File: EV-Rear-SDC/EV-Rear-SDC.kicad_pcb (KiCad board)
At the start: 2 copper layers, 0 parts

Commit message: Moved Mosfet to avoid EMI error
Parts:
- added C1: 0.1u, Capacitor_SMD:C_0805_2012Metric, F.Cu at (104.6, 125.0)
- added C2: 0.1u, Capacitor_SMD:C_0805_2012Metric, F.Cu at (85.0, 131.6)
- added C3: 1u, Capacitor_SMD:C_0805_2012Metric, F.Cu at (104.7, 128.7)
- added C4: 10u, Capacitor_SMD:C_0805_2012Metric, F.Cu at (85.1, 134.9)
- added C5: 1u, Capacitor_SMD:C_0805_2012Metric, F.Cu at (104.7, 132.3)
- added C6: 0.1u, Capacitor_SMD:C_0805_2012Metric, F.Cu at (73.8, 121.4)
- added C7: 0.1u, Capacitor_SMD:C_0805_2012Metric, F.Cu at (101.2, 116.8)
- added C8: 1u, Capacitor_SMD:C_0805_2012Metric, F.Cu at (101.3, 120.2)
- added C9: 0.1u, Capacitor_SMD:C_0805_2012Metric, F.Cu at (85.0, 117.7)
- added D1: LED, LED_SMD:LED_0805_2012Metric, F.Cu at (87.3, 109.5)
- added D2: LED, LED_SMD:LED_0805_2012Metric, F.Cu at (77.0, 109.1)
- added D3: LED, LED_SMD:LED_0805_2012Metric, F.Cu at (70.3, 109.2)
- added D4: LED, LED_SMD:LED_0805_2012Metric, F.Cu at (66.6, 121.4)
- added D5: LED, LED_SMD:LED_0805_2012Metric, F.Cu at (66.6, 128.7)
- added D6: D, Diode_SMD:D_0805_2012Metric, F.Cu at (105.0, 143.2)
- added D7: LED, LED_SMD:LED_0805_2012Metric, F.Cu at (66.2, 135.5)
- added D8: LED, LED_SMD:LED_0805_2012Metric, F.Cu at (76.1, 133.7)
- added D9: LED, LED_SMD:LED_0805_2012Metric, F.Cu at (81.0, 133.4)
- added G***: LOGO, LOGO, F.Cu at (106.5, 95.0)
- added J1: JST-XA, Custom_MSM:JST_XA_S02B-XASK-1_1x02_P2.50mm_Horizontal, F.Cu at (94.7, 100.2)
- added J2: B06B-PASK_LF__SN_, Custom_MSM:S06BXASK1LFSN, F.Cu at (82.1, 100.3)
- added J3: B08B-XASK-1_LF__SN_, Custom_MSM:S08BXASK1LFSN, F.Cu at (58.0, 119.3)
- added J4: S5B-XH-A-1_LF__SN_, Custom_MSM:S5BXHA1LFSN, F.Cu at (56.8, 102.8)
- added J5: Conn_01x14, Custom_MSM:JST_XA_S14B-XASK-1_1x14_P2.50mm_Horizontal, F.Cu at (108.2, 136.0)
- added K1: Relay_SPDT_G6RN, Custom_MSM:Relay_SPDT_G6RN, F.Cu at (98.6, 139.3)
- added Q1: BSS205N, Custom_MSM:MOSFET_Single_SOT-23, B.Cu at (87.6, 111.1)
- added Q2: BSS205N, Custom_MSM:MOSFET_Single_SOT-23, B.Cu at (77.1, 110.3)
- added Q3: BSS205N, Custom_MSM:MOSFET_Single_SOT-23, B.Cu at (70.5, 110.7)
- added Q4: BSS205N, Custom_MSM:MOSFET_Single_SOT-23, B.Cu at (67.4, 121.5)
- added Q5: BSS205N, Custom_MSM:MOSFET_Single_SOT-23, B.Cu at (67.3, 128.4)
- added Q6: BSS205N, Custom_MSM:MOSFET_Single_SOT-23, F.Cu at (110.5, 143.2)
- added Q7: BSS205N, Custom_MSM:MOSFET_Single_SOT-23, B.Cu at (67.0, 135.6)
- added Q8: BSS205N, Custom_MSM:MOSFET_Single_SOT-23, B.Cu at (76.1, 132.7)
- added Q9: BSS205N, Custom_MSM:MOSFET_Single_SOT-23, B.Cu at (66.8, 145.4)
- added R1: 300, Resistor_SMD:R_0805_2012Metric, F.Cu at (87.4, 113.1)
- added R10: 75K, Resistor_SMD:R_0805_2012Metric, B.Cu at (67.6, 108.0)
- added R11: 25k, Resistor_SMD:R_0805_2012Metric, B.Cu at (67.5, 113.4)
- added R12: 300, Resistor_SMD:R_0805_2012Metric, F.Cu at (70.2, 121.4)
- added R13: 75K, Resistor_SMD:R_0805_2012Metric, B.Cu at (64.6, 124.6)
- added R14: 25k, Resistor_SMD:R_0805_2012Metric, B.Cu at (70.1, 124.5)
- added R15: 300, Resistor_SMD:R_0805_2012Metric, F.Cu at (70.1, 128.7)
- added R16: 75K, Resistor_SMD:R_0805_2012Metric, B.Cu at (64.5, 131.3)
- added R17: 25k, Resistor_SMD:R_0805_2012Metric, B.Cu at (70.2, 131.2)
- added R18: 300, Resistor_SMD:R_0805_2012Metric, F.Cu at (69.8, 135.5)
- added R19: 100k, Resistor_SMD:R_0805_2012Metric, F.Cu at (113.5, 146.2)
- added R2: 75K, Resistor_SMD:R_0805_2012Metric, B.Cu at (83.7, 108.7)
- added R20: 75K, Resistor_SMD:R_0805_2012Metric, B.Cu at (64.2, 138.5)
- added R21: 25k, Resistor_SMD:R_0805_2012Metric, B.Cu at (69.8, 138.6)
- added R22: 300, Resistor_SMD:R_0805_2012Metric, F.Cu at (76.1, 130.2)
- added R23: 75K, Resistor_SMD:R_0805_2012Metric, B.Cu at (79.0, 136.0)
- added R24: 25k, Resistor_SMD:R_0805_2012Metric, B.Cu at (79.1, 129.6)
- added R25: 300, Resistor_SMD:R_0805_2012Metric, F.Cu at (81.0, 129.8)
- added R26: 75K, Resistor_SMD:R_0805_2012Metric, B.Cu at (63.8, 141.4)
- added R27: 25k, Resistor_SMD:R_0805_2012Metric, B.Cu at (70.0, 141.4)
- added R3: 10k, Resistor_SMD:R_0805_2012Metric, F.Cu at (85.0, 121.7)
- added R4: 25k, Resistor_SMD:R_0805_2012Metric, B.Cu at (83.7, 113.3)
- added R5: 10k, Resistor_SMD:R_0805_2012Metric, F.Cu at (85.0, 119.8)
- added R6: 300, Resistor_SMD:R_0805_2012Metric, F.Cu at (77.1, 112.8)
- added R7: 75K, Resistor_SMD:R_0805_2012Metric, B.Cu at (74.3, 107.8)
- added R8: 25k, Resistor_SMD:R_0805_2012Metric, B.Cu at (74.4, 113.0)
- added R9: 300, Resistor_SMD:R_0805_2012Metric, F.Cu at (70.3, 112.9)
- added REF**: Board_Small_Outer-Mounting, Custom_MSM:Board_Small_Outer-Mounting, F.Cu at (87.4, 119.7)
- added U1: SCH16T-K01-10, Custom_MSM:SCH16TK0110, F.Cu at (94.6, 130.0)
- added U2: ~, Package_DFN_QFN:QFN-24-1EP_4x4mm_P0.5mm_EP2.7x2.7mm, F.Cu at (78.9, 122.2)
- added U3: MAX3390EEUD_T, Custom_MSM:SOP65P640X110-14N, F.Cu at (94.4, 118.7)
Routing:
- net Inverter_high: track 0.00 -> 160.8 mm, vias 0 -> 5
- net Inverter_low: track 0.00 -> 73.9 mm
- net Relay_out: track 0.00 -> 72.1 mm
- net +3V3: track 0.00 -> 66.7 mm, vias 0 -> 1
- net +24V: track 0.00 -> 59.6 mm
- net 5V_SCLK: track 0.00 -> 48.6 mm, vias 0 -> 2
- net IMD/AMS_IN: track 0.00 -> 44.7 mm
- net GND: track 0.00 -> 44.0 mm, vias 0 -> 16
- net Inverter_S: track 0.00 -> 41.5 mm, vias 0 -> 3
- net 5V_MISO: track 0.00 -> 41.5 mm, vias 0 -> 2
- net 5V_MOSI: track 0.00 -> 37.0 mm, vias 0 -> 2
- net 5V_CS_C: track 0.00 -> 36.7 mm
- net BSPD: track 0.00 -> 29.7 mm
- net HVD_S: track 0.00 -> 27.4 mm, vias 0 -> 2
- net PTSDIL_S: track 0.00 -> 27.3 mm, vias 0 -> 2
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- added copper zone on B.Cu, net GND
- added copper zone on F.Cu, net GND
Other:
- board outline added: 78 x 58 mm

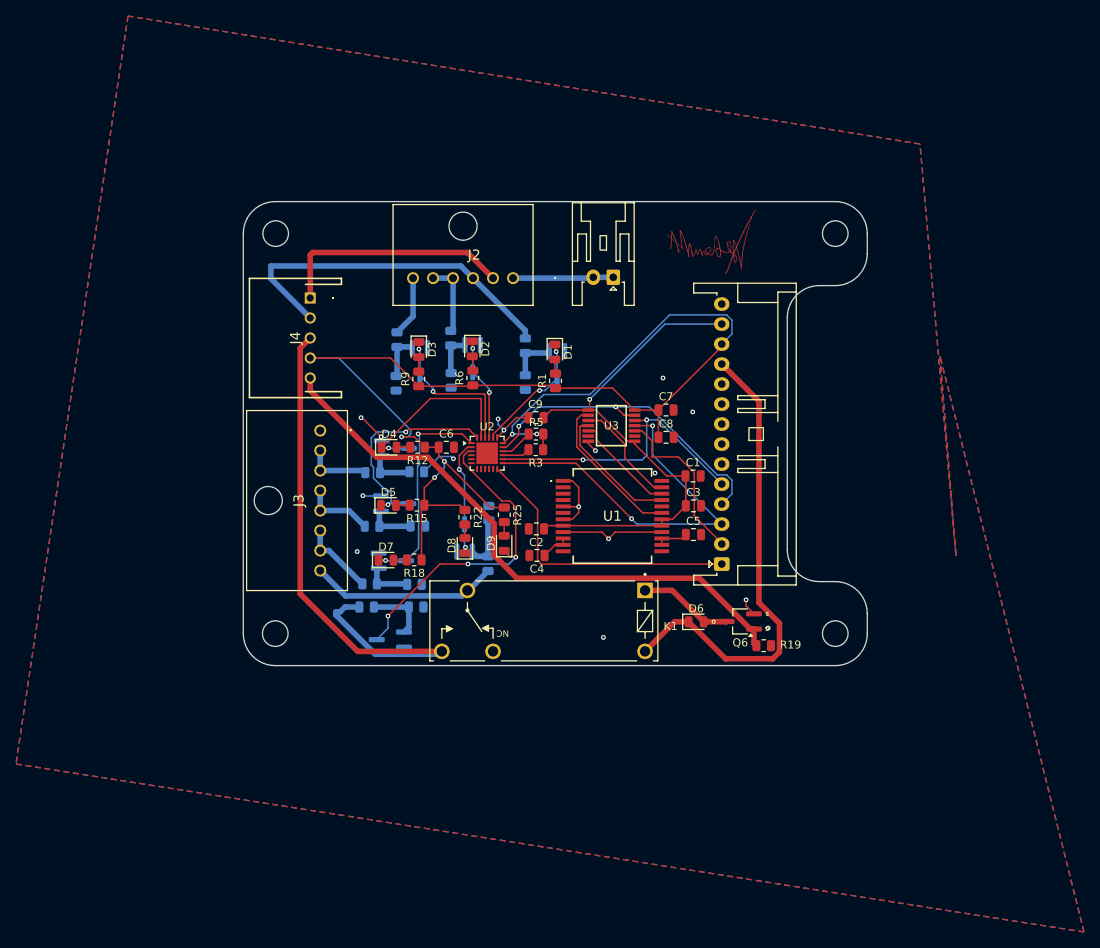
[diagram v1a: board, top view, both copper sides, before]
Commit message: Re-routed and did full CC bom for rear
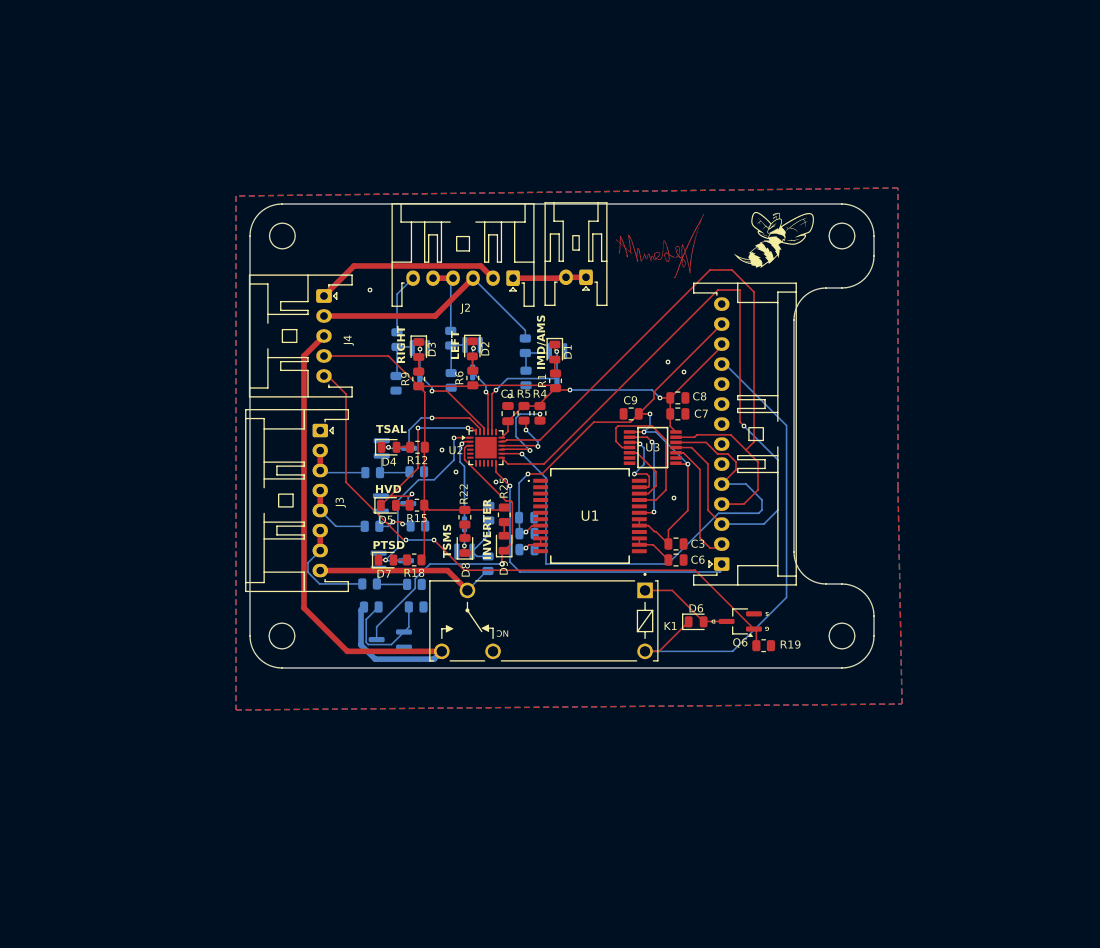
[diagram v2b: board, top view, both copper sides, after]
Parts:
- removed the G*** at (106.5, 95.0)
- added G***: LOGO, LOGO, F.Cu at (100.1, 95.5)
- added G***: LOGO, LOGO, B.Cu at (100.0, 121.8)
- added REF**: LOGO, Custom_MSM:Decorative_Stinger, F.Cu at (114.8, 95.5)
- C2: moved to B.Cu
- C3: value 1u -> 0.1u
- C4: value 10u -> 1u; moved to B.Cu
- C5: value 1u -> 10u; moved to B.Cu
- C6: value 0.1u -> 1u
- J2: value B06B-PASK_LF__SN_ -> Conn_01x06; footprint Custom_MSM:S06BXASK1LFSN -> Connector_JST:JST_XA_S06B-XASK-1_1x06_P2.50mm_Horizontal
- J3: value B08B-XASK-1_LF__SN_ -> Conn_01x08; footprint Custom_MSM:S08BXASK1LFSN -> Connector_JST:JST_XA_S08B-XASK-1_1x08_P2.50mm_Horizontal
- J4: value S5B-XH-A-1_LF__SN_ -> Conn_01x05; footprint Custom_MSM:S5BXHA1LFSN -> Connector_JST:JST_XA_S05B-XASK-1_1x05_P2.50mm_Horizontal
- R1, R12, R15, R18, R22, R25, R6, R9: value 300 -> 300R
- R3: value 10k -> 25k; moved to B.Cu
- R4: value 25k -> 10k; moved to F.Cu
- moved C6 32.0 mm to (102.5, 135.5)
- moved C1 24.4 mm to (81.5, 117.2), turned to 90 degrees
- moved C5 20.9 mm to (83.9, 134.2)
- moved C9 11.9 mm to (96.9, 117.2)
- moved R3 9.04 mm to (83.8, 112.8), turned to 90 degrees
- moved U3 5.86 mm to (99.6, 121.5)
- moved C3 5.24 mm to (102.5, 133.5)
- moved C8 5.13 mm to (102.7, 115.2)
- moved R4 4.26 mm to (85.5, 117.2), turned to -90 degrees
- moved J1 3.41 mm to (91.2, 100.2)
- moved R5 3.00 mm to (83.5, 117.2), turned to -90 degrees
- moved C4 3.00 mm to (83.9, 132.2), turned to 0 degrees
- moved U1 2.81 mm to (91.8, 130.0)
- moved C2 1.86 mm to (83.8, 130.2), turned to 0 degrees
- moved J4 1.74 mm to (58.5, 102.5), turned to -90 degrees
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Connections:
- C1 pad 1: +3V3 -> Inverter_high
- C4 pad 1: Net-(U1-VREGA) -> +3V3
- C5 pad 1: Net-(U1-VREGD) -> Net-(U1-VREGA)
- C6 pad 1: Inverter_high -> Net-(U1-VREGD)
- D4 pad 1: TSAL_S -> unconnected-(D4-K-Pad1)
- D4 pad 2: Net-(D4-A) -> unconnected-(D4-A-Pad2)
- R12 pad 2: Net-(D4-A) -> unconnected-(R12-Pad2)
- R3 pad 1: Inverter_high -> GND
- R3 pad 2: Net-(U2-RESET) -> Net-(Q1-G)
- R4 pad 1: GND -> Inverter_high
- R4 pad 2: Net-(Q1-G) -> Net-(U2-RESET)
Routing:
- net Inverter_high: track 160.8 -> 102.3 mm, vias 5 -> 2
- net GND: track 44.0 -> 0.00 mm, vias 16 -> 8
- net 5V_MISO: track 41.5 -> 82.3 mm, vias 2 -> 0
- net 5V_SCLK: track 48.6 -> 89.4 mm, vias 2 -> 1
- net 5V_MOSI: track 37.0 -> 66.5 mm, vias 2 -> 1
- net IMD/AMS_IN: track 44.7 -> 30.8 mm
- net Net-(U2-RESET): track 3.49 -> 12.4 mm, vias 0 -> 2
- net +3V3: track 66.7 -> 74.3 mm, vias 1 -> 5
- net TSAL_S: track 23.3 -> 16.2 mm, vias 1 -> 2
- net BSPD: track 29.7 -> 23.3 mm
- net Net-(Q9-G): track 7.75 -> 13.9 mm
- net MISO: track 19.1 -> 13.8 mm, vias 0 -> 2
- net 5V_CS_D: track 21.1 -> 15.9 mm
- net CS_D: track 13.0 -> 8.54 mm
- net Net-(U2-INT): track 4.12 -> 8.54 mm, vias 0 -> 2
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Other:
- board text added: "HVD"
- board text added: "IMD/AMS"
- board text added: "INVERTER"
- board text added: "LEFT"
- board text added: "PTSD"
- board text added: "RIGHT"
- board text added: "Rear SDC V1.0 Designed by Ahmed Kandil Routed 27/10/2026"
- board text added: "TSAL"
- board text added: "TSMS"

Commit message: Added stuff to BOM
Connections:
- D4 pad 1: unconnected-(D4-K-Pad1) -> TSAL_S
- D4 pad 2: unconnected-(D4-A-Pad2) -> Net-(D4-A)
- R12 pad 2: unconnected-(R12-Pad2) -> Net-(D4-A)
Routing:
- net Net-(D4-A): track 0.00 -> 1.71 mm
- net (no net): track 1.71 -> 0.00 mm
